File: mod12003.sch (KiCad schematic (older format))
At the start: 34 parts, among them J1 IN, J2 OUT, J3 24V, J4 OUT+, J5 OUT-, J8 DEVEL, Q1 AO4805, Q2 12A

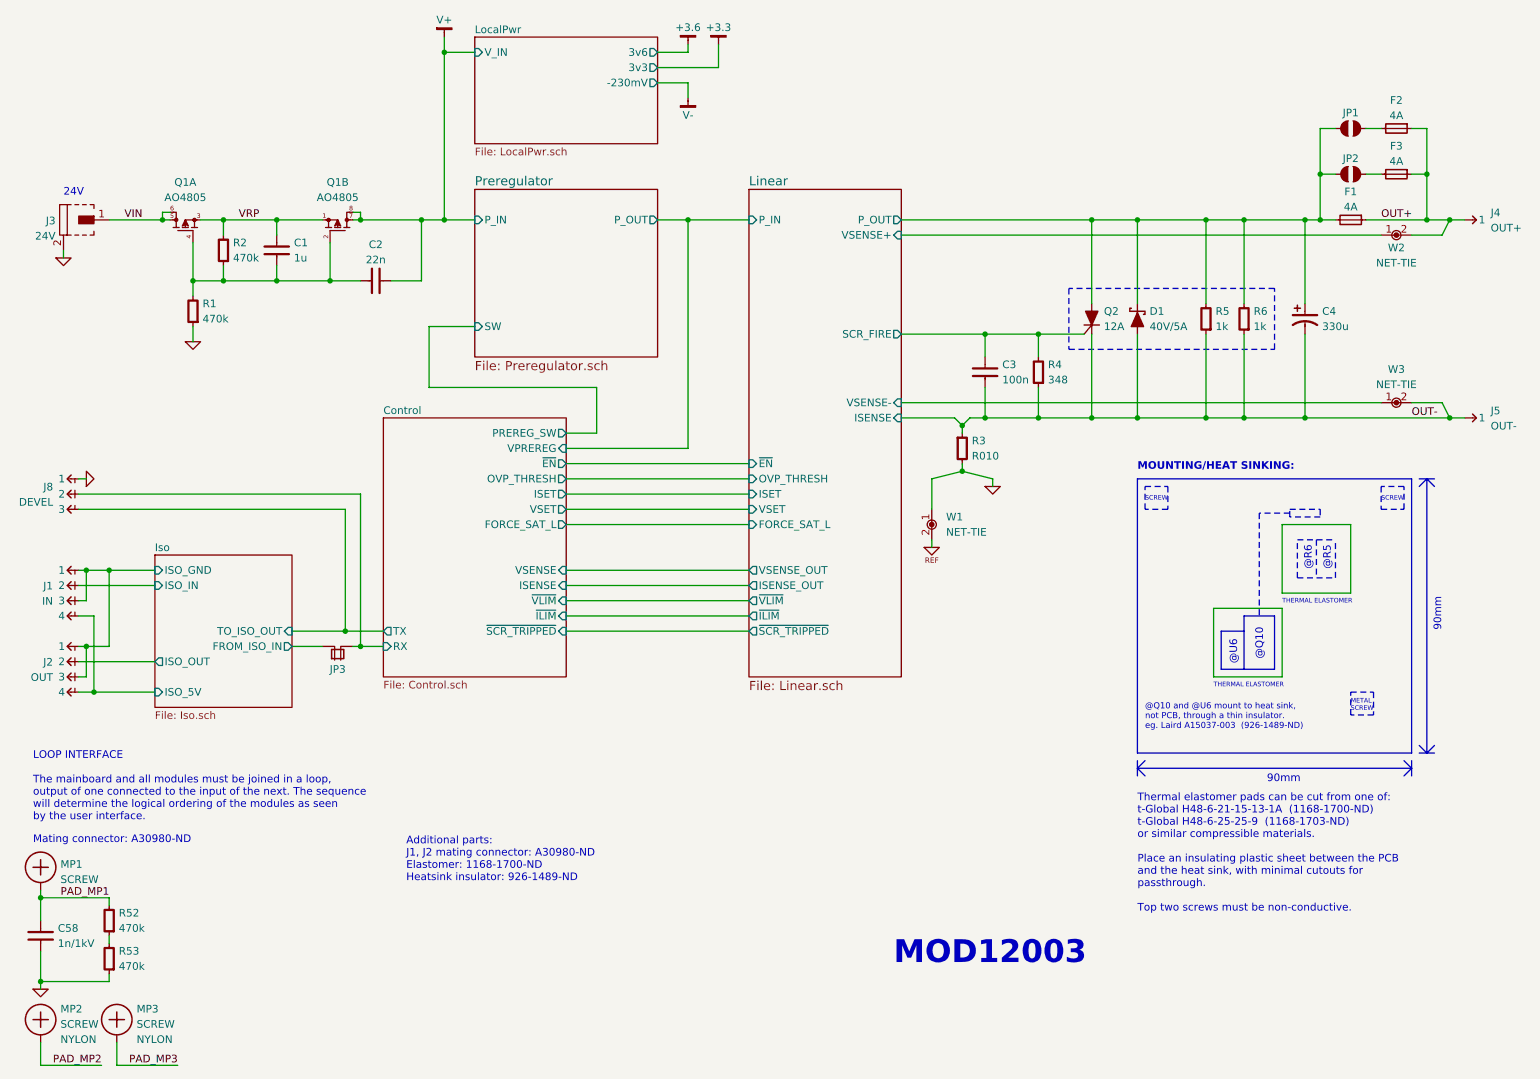
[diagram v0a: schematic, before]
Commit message: Remove comments about insulating screws
Final PCB used insulated pads
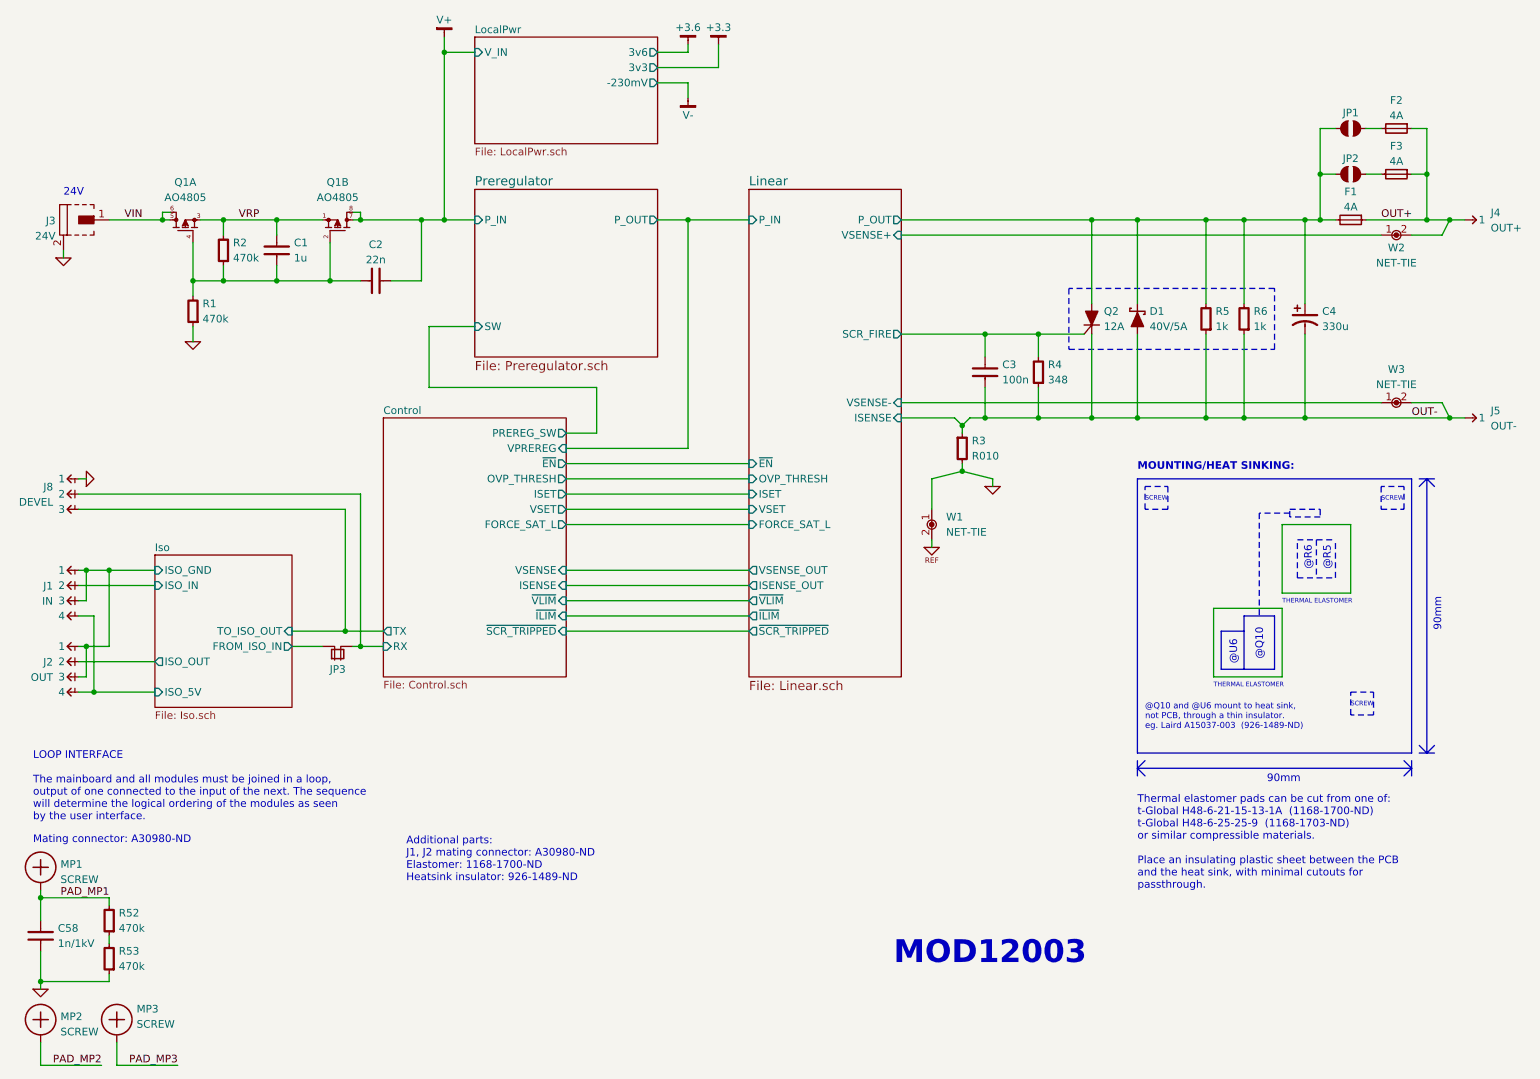
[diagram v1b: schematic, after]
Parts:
- MP2, MP3: Value2 NYLON -> (none)
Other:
- note added: "Thermal elastomer pads can be cut from one of:\nt-Global H48-6-21-15-13-1A (1168-1700-ND)\nt-Global H48-6-25-25-9 (1168-1703-ND)\nor similar compressible materials.\n\nPlace an insulating plastic sheet between the PCB\nand the heat sink, with minimal cutouts for\npassthrough."
- note removed: "METAL\nSCREW"
- note removed: "Thermal elastomer pads can be cut from one of:\nt-Global H48-6-21-15-13-1A (1168-1700-ND)\nt-Global H48-6-25-25-9 (1168-1703-ND)\nor similar compressible materials.\n\nPlace an insulating plastic sheet between the PCB\nand the heat sink, with minimal cutouts for\npassthrough.\n\nTop two screws must be non-conductive."
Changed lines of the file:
@@
 U 1 1 55CD1961
 P 750 7650
-F 0 "MP2" H 880 7720 50  0000 L CNN
-F 1 "SCREW" H 880 7620 50  0000 L CNN
+F 0 "MP2" H 880 7670 50  0000 L CNN
+F 1 "SCREW" H 880 7570 50  0000 L CNN
 F 2 "mech:SCREW-4-SUPPORTED" H 750 7650 50  0001 C CNN
 F 3 "" H 750 7650 60  0000 C CNN
-F 4 "NYLON" H 880 7520 50  0000 L CNN "Value2"
+F 4 "~" H 880 7520 50  0000 L CNN "Value2"
 	1    750  7650
 	1    0    0    -1
@@
 Text Notes 9550 4250 0    30   ~ 0
 SCREW
-Text Notes 9350 5630 0    30   ~ 0
-METAL\nSCREW
+Text Notes 9350 5600 0    30   ~ 0
+SCREW
 Text Notes 8900 4925 0    30   ~ 0
 THERMAL ELASTOMER
 Text Notes 8450 5475 0    30   ~ 0
 THERMAL ELASTOMER
-Text Notes 7950 6950 0    50   ~ 0
-Thermal elastomer pads can be cut from one of:\nt-Global H48-6-21-15-13-1A  (1168-1700-ND)\nt-Global H48-6-25-25-9  (1168-1703-ND)\nor similar compressible materials.\n\nPlace an insulating plastic sheet between the PCB\nand the heat sink, with minimal cutouts for\npassthrough.\n\nTop two screws must be non-conductive.
+Text Notes 7950 6800 0    50   ~ 0
+Thermal elastomer pads can be cut from one of:\nt-Global H48-6-21-15-13-1A  (1168-1700-ND)\nt-Global H48-6-25-25-9  (1168-1703-ND)\nor similar compressible materials.\n\nPlace an insulating plastic sheet between the PCB\nand the heat sink, with minimal cutouts for\npassthrough.
 Wire Wire Line
 	10000 2400 9950 2500
@@
 F 2 "mech:SCREW-4-SUPPORTED" H 1250 7650 50  0001 C CNN
 F 3 "" H 1250 7650 60  0000 C CNN
-F 4 "NYLON" H 1380 7520 50  0000 L CNN "Value2"
+F 4 "~" H 1380 7520 50  0000 L CNN "Value2"
 	1    1250 7650
 	1    0    0    -1
